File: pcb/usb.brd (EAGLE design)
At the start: 26.2 x 26.2 mm, 27 parts, among them J1 JSTPH, Q1 ZXMP6A13FTA, Q2 mmbt2222, Q3 mmbt2222, U1 MIC5225-3.3v, U2 CH340C, U3 MCP73831T-2ACI/OT, X1 SM02B-SRSS-TB

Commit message: Headers were on the wrong side on the usb board
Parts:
- flipped JP1 to the top
- flipped JP2 to the top
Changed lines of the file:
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@@
 <attribute name="VALUE" x="7.6835" y="9.144" size="0.4064" layer="27" rot="R270"/>
 </element>
-<element name="JP2" library="adafruit" library_urn="urn:adsk.eagle:library:420" package="1X08-CLEANBIG" package3d_urn="urn:adsk.eagle:package:6240708/1" override_package3d_urn="urn:adsk.eagle:package:21520758/2" override_package_urn="urn:adsk.eagle:footprint:6240062/1" value="" x="1.651" y="13.081" smashed="yes" rot="MR90">
-<attribute name="MPN" value="8Fx1L-254mm" x="1.651" y="13.081" size="1.778" layer="28" rot="MR90" display="off"/>
-<attribute name="VALUE" x="-1.524" y="2.921" size="1.27" layer="28" rot="MR90"/>
-</element>
-<element name="JP1" library="adafruit" library_urn="urn:adsk.eagle:library:420" package="1X08-CLEANBIG" package3d_urn="urn:adsk.eagle:package:6240708/1" override_package3d_urn="urn:adsk.eagle:package:21520677/2" override_package_urn="urn:adsk.eagle:footprint:6240062/1" value="" x="24.511" y="13.081" smashed="yes" rot="MR270">
-<attribute name="MPN" value="8Fx1L-254mm" x="24.511" y="13.081" size="1.778" layer="28" rot="MR270" display="off"/>
-<attribute name="VALUE" x="27.686" y="23.241" size="1.27" layer="28" rot="MR270"/>
+<element name="JP2" library="adafruit" library_urn="urn:adsk.eagle:library:420" package="1X08-CLEANBIG" package3d_urn="urn:adsk.eagle:package:6240708/1" override_package3d_urn="urn:adsk.eagle:package:21520758/2" override_package_urn="urn:adsk.eagle:footprint:6240062/1" value="" x="1.651" y="13.081" smashed="yes" rot="R90">
+<attribute name="MPN" value="8Fx1L-254mm" x="1.651" y="13.081" size="1.778" layer="27" rot="R90" display="off"/>
+<attribute name="VALUE" x="4.826" y="2.921" size="1.27" layer="27" rot="R90"/>
+</element>
+<element name="JP1" library="adafruit" library_urn="urn:adsk.eagle:library:420" package="1X08-CLEANBIG" package3d_urn="urn:adsk.eagle:package:6240708/1" override_package3d_urn="urn:adsk.eagle:package:21520677/2" override_package_urn="urn:adsk.eagle:footprint:6240062/1" value="" x="24.511" y="13.081" smashed="yes" rot="R270">
+<attribute name="MPN" value="8Fx1L-254mm" x="24.511" y="13.081" size="1.778" layer="27" rot="R270" display="off"/>
+<attribute name="VALUE" x="21.336" y="23.241" size="1.27" layer="27" rot="R270"/>
 </element>
 <element name="J2" library="Wurth_Elektronik_Electromechanic_Input-Output_Connectors_rev19b_wider_slots" package="614105150621" package3d_urn="urn:adsk.eagle:package:3360156/4" override_package3d_urn="urn:adsk.eagle:package:21520771/2" override_package_urn="urn:adsk.eagle:footprint:21520772/1" value="" x="13.081" y="2.54" smashed="yes" rot="MR0">
@@
 <wire x1="20.0025" y1="18.0975" x2="18.89125" y2="16.98625" width="0.1524" layer="16"/>
 <wire x1="23.1775" y1="18.0975" x2="20.0025" y2="18.0975" width="0.1524" layer="16"/>
-<wire x1="24.28875" y1="19.20875" x2="23.1775" y2="18.0975" width="0.1524" layer="16"/>
-<wire x1="24.28875" y1="19.3675" x2="24.28875" y2="19.20875" width="0.1524" layer="16"/>
-<wire x1="24.4475" y1="19.3675" x2="24.28875" y2="19.3675" width="0.1524" layer="16"/>
-<wire x1="24.4475" y1="19.3675" x2="24.511" y2="19.431" width="0.1524" layer="16"/>
 <via x="16.51" y="12.22375" extent="1-16" drill="0.254"/>
+<wire x1="24.511" y1="19.431" x2="23.1775" y2="18.0975" width="0.1524" layer="16"/>
 </signal>
 <signal name="TX">
@@
 <wire x1="18.51025" y1="20.6375" x2="18.38325" y2="20.5105" width="0.1524" layer="16"/>
 <wire x1="23.1775" y1="20.6375" x2="18.51025" y2="20.6375" width="0.1524" layer="16"/>
-<wire x1="24.28875" y1="21.74875" x2="23.1775" y2="20.6375" width="0.1524" layer="16"/>
-<wire x1="24.28875" y1="21.9075" x2="24.28875" y2="21.74875" width="0.1524" layer="16"/>
-<wire x1="24.4475" y1="21.9075" x2="24.28875" y2="21.9075" width="0.1524" layer="16"/>
 <wire x1="14.605" y1="7.62" x2="14.605" y2="7.614" width="0.1524" layer="1"/>
-<wire x1="24.4475" y1="21.9075" x2="24.511" y2="21.971" width="0.1524" layer="16"/>
 <via x="17.145" y="11.90625" extent="1-16" drill="0.254"/>
 <via x="20.32" y="15.08125" extent="1-16" drill="0.254"/>
@@
 <wire x1="19.0044" y1="16.1906" x2="20.0956875" y2="16.1906" width="0.1524" layer="1"/>
 <wire x1="17.8689" y1="17.7259" x2="17.8689" y2="17.3261" width="0.1524" layer="1"/>
+<wire x1="24.511" y1="21.971" x2="23.1775" y2="20.6375" width="0.1524" layer="16"/>
 </signal>
 <signal name="RESET">
@@
 <wire x1="3.4925" y1="20.16125" x2="3.4925" y2="17.4625" width="0.1524" layer="16"/>
 <wire x1="1.905" y1="21.74875" x2="3.4925" y2="20.16125" width="0.1524" layer="16"/>
-<wire x1="1.905" y1="21.9075" x2="1.905" y2="21.74875" width="0.1524" layer="16"/>
-<wire x1="1.74625" y1="21.9075" x2="1.905" y2="21.9075" width="0.1524" layer="16"/>
 <wire x1="4.1275" y1="11.90625" x2="4.234" y2="11.811" width="0.1524" layer="1"/>
-<wire x1="1.74625" y1="21.9075" x2="1.651" y2="21.971" width="0.1524" layer="16"/>
 <via x="3.96875" y="16.8275" extent="1-16" drill="0.254"/>
+<wire x1="1.651" y1="21.971" x2="1.87325" y2="21.74875" width="0.1524" layer="16"/>
+<wire x1="1.87325" y1="21.74875" x2="1.905" y2="21.74875" width="0.1524" layer="16"/>
 </signal>
 <signal name="RTS">
@@
 <wire x1="24.4475" y1="11.7475" x2="18.0975" y2="11.7475" width="0.1524" layer="16"/>
 <wire x1="9.04875" y1="8.09625" x2="8.974" y2="8.128" width="0.1524" layer="1"/>
-<wire x1="24.4475" y1="11.7475" x2="24.511" y2="11.811" width="0.1524" layer="16"/>
 <via x="9.8425" y="8.09625" extent="1-16" drill="0.254"/>
 <via x="17.78" y="9.04875" extent="1-16" drill="0.254"/>
 <via x="17.93875" y="11.58875" extent="1-16" drill="0.254"/>
+<wire x1="24.511" y1="11.811" x2="24.4475" y2="11.7475" width="0.1524" layer="16"/>
 </signal>
 <signal name="D4/GPIO2">
@@
 <wire x1="6.985" y1="20.0025" x2="6.8881" y2="19.997" width="0.4064" layer="1"/>
 <wire x1="7.14375" y1="17.93875" x2="6.8881" y2="18.097" width="0.4064" layer="1"/>
-<wire x1="23.65375" y1="4.1275" x2="24.4475" y2="4.1275" width="0.4064" layer="16"/>
+<wire x1="24.4475" y1="4.1275" x2="23.65375" y2="4.1275" width="0.4064" layer="16"/>
 <wire x1="17.145" y1="10.63625" x2="23.65375" y2="4.1275" width="0.4064" layer="16"/>
 <wire x1="16.03375" y1="10.63625" x2="17.145" y2="10.63625" width="0.4064" layer="16"/>
 <wire x1="15.5575" y1="11.1125" x2="16.03375" y2="10.63625" width="0.4064" layer="16"/>
 <wire x1="15.5575" y1="12.22375" x2="15.5575" y2="11.1125" width="0.4064" layer="16"/>
-<wire x1="24.4475" y1="4.1275" x2="24.511" y2="4.191" width="0.4064" layer="16"/>
 <wire x1="15.5575" y1="12.22375" x2="15.581" y2="12.35" width="0.4064" layer="16"/>
 <via x="6.985" y="14.2875" extent="1-16" drill="0.254"/>
@@
 <wire x1="7.151" y1="16.002" x2="7.151" y2="14.4535" width="0.4064" layer="1"/>
 <wire x1="7.151" y1="14.4535" x2="6.985" y2="14.2875" width="0.4064" layer="1"/>
+<wire x1="24.511" y1="4.191" x2="24.4475" y2="4.1275" width="0.4064" layer="16"/>
 </signal>
 <signal name="N$2">
@@
 <wire x1="10.61085" y1="10.1346" x2="9.58999375" y2="10.1346" width="0.4064" layer="16"/>
 <wire x1="9.2329" y1="9.77750625" x2="9.2329" y2="9.7409" width="0.4064" layer="16"/>
-<wire x1="3.683" y1="4.191" x2="1.651" y2="4.191" width="0.4064" layer="16"/>
-<wire x1="9.2329" y1="9.7409" x2="3.683" y2="4.191" width="0.4064" layer="16"/>
+<wire x1="3.683" y1="4.191" x2="9.2329" y2="9.7409" width="0.4064" layer="16"/>
 <wire x1="12.054" y1="14.986" x2="12.065" y2="14.975" width="0.4064" layer="1"/>
 <wire x1="12.065" y1="14.975" x2="12.065" y2="13.214" width="0.4064" layer="1"/>
+<wire x1="1.651" y1="4.191" x2="3.683" y2="4.191" width="0.4064" layer="16"/>
 </signal>
 </signals>

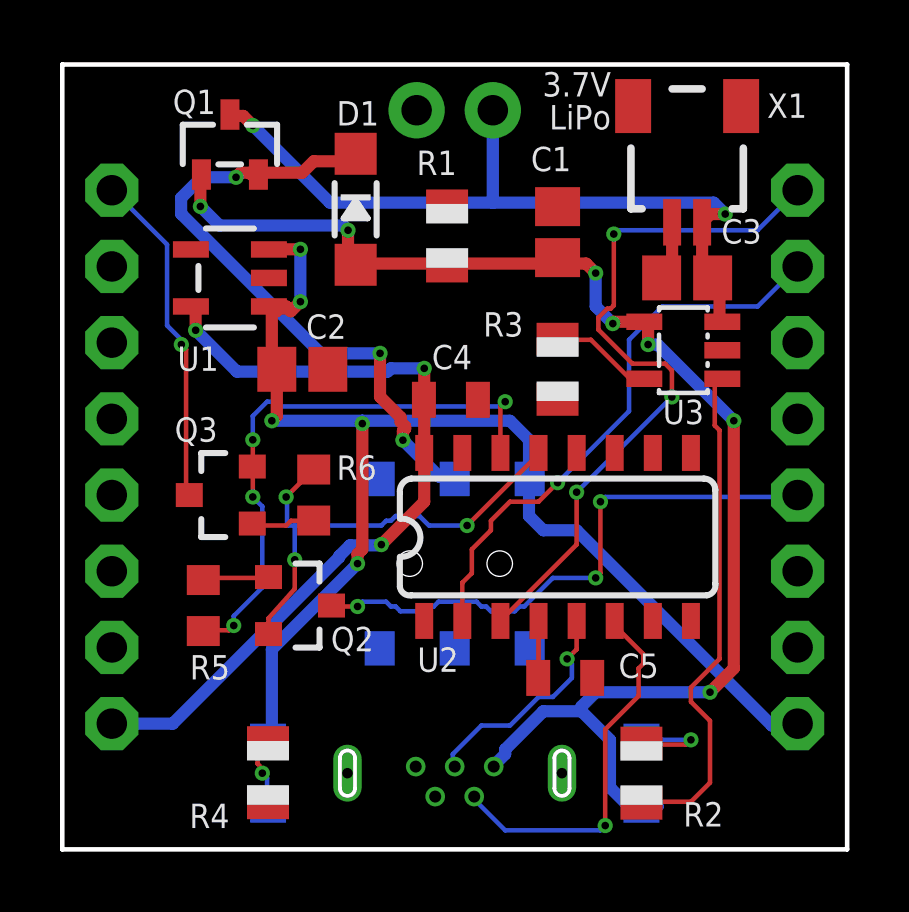
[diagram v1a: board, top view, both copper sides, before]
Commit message: Rotate switch so that pin numbering matches orientation from the datasheet
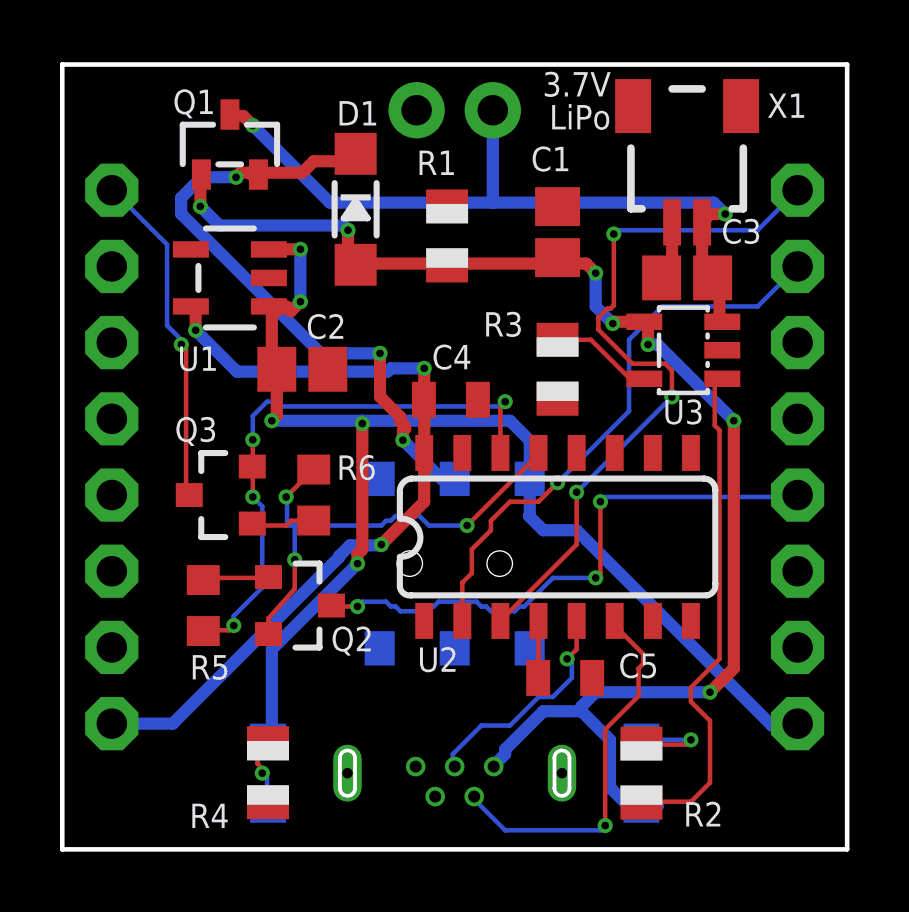
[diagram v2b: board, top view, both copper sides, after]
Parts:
- turned S1 to 180 degrees
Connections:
- net N$7: now also S1.5; no longer S1.2
- net VIN: now also S1.6; no longer S1.1
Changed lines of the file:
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@@
 <attribute name="VALUE" x="7.366" y="22.86" size="0.4064" layer="27" ratio="10"/>
 </element>
-<element name="S1" library="SparkFun-Switches" library_urn="urn:adsk.eagle:library:535" package="SWITCH_DPDT_SMD_AYZ0202" package3d_urn="urn:adsk.eagle:package:40160/1" override_package3d_urn="urn:adsk.eagle:package:21520767/2" override_package_urn="urn:adsk.eagle:footprint:40100/1" value="" x="13.081" y="9.525" smashed="yes" rot="MR0">
-<attribute name="MPN" value="AYZ0202AGRLC" x="13.081" y="9.525" size="1.778" layer="28" rot="MR0" display="off"/>
-<attribute name="NAME" x="17.018" y="11.811" size="0.8128" layer="26" ratio="18" rot="MR0" align="bottom-center"/>
-<attribute name="PROD_ID" value="SWCH-08179" x="13.081" y="9.525" size="1.778" layer="28" rot="MR0" display="off"/>
-<attribute name="SF_ID" value="COM-00597" x="13.081" y="9.525" size="1.778" layer="28" rot="MR0" display="off"/>
-<attribute name="VALUE" x="9.271" y="9.525" size="0.6096" layer="28" font="vector" ratio="20" rot="MR90" align="top-center"/>
+<element name="S1" library="SparkFun-Switches" package="SWITCH_DPDT_SMD_AYZ0202" package3d_urn="urn:adsk.eagle:package:40160/1" override_package3d_urn="urn:adsk.eagle:package:21520767/4" override_package_urn="urn:adsk.eagle:footprint:40100/1" override_locally_modified="yes" value="" x="13.081" y="9.525" smashed="yes" rot="MR180">
+<attribute name="MPN" value="AYZ0202AGRLC" x="13.081" y="9.525" size="1.778" layer="28" rot="MR180" display="off"/>
+<attribute name="NAME" x="16.891" y="12.573" size="0.8128" layer="26" ratio="18" rot="MR180" align="bottom-center"/>
+<attribute name="PROD_ID" value="SWCH-08179" x="13.081" y="9.525" size="1.778" layer="28" rot="MR180" display="off"/>
+<attribute name="SF_ID" value="COM-00597" x="13.081" y="9.525" size="1.778" layer="28" rot="MR180" display="off"/>
+<attribute name="VALUE" x="16.891" y="9.525" size="0.6096" layer="28" font="vector" ratio="20" rot="MR270" align="top-center"/>
 </element>
 <element name="U2" library="SparkFun-IC-Comms" library_urn="urn:adsk.eagle:library:521" package="SO016" value="CH340C" x="16.51" y="10.414" smashed="yes">
@@
 <contactref element="D1" pad="C"/>
 <contactref element="Q1" pad="2"/>
-<contactref element="S1" pad="2"/>
+<contactref element="S1" pad="5"/>
 <wire x1="8.001" y1="22.5552" x2="6.5532" y2="22.5552" width="0.4064" layer="1"/>
 <wire x1="8.382" y1="22.9362" x2="8.001" y2="22.5552" width="0.4064" layer="1"/>
@@
 <wire x1="6.5532" y1="22.5552" x2="6.538" y2="22.495" width="0.4064" layer="1"/>
 <wire x1="9.7536" y1="23.1648" x2="9.779" y2="23.186" width="0.4064" layer="1"/>
-<wire x1="12.573" y1="12.4206" x2="13.0302" y2="12.4206" width="0.4064" layer="16"/>
-<wire x1="11.3538" y1="13.6398" x2="12.573" y2="12.4206" width="0.4064" layer="16"/>
 <wire x1="11.3538" y1="13.9446" x2="11.3538" y2="13.6398" width="0.4064" layer="1"/>
 <wire x1="11.43" y1="14.0208" x2="11.3538" y2="13.9446" width="0.4064" layer="1"/>
@@
 <wire x1="6.2484" y1="22.5552" x2="5.9436" y2="22.5552" width="0.4064" layer="1"/>
 <wire x1="6.3246" y1="22.479" x2="6.2484" y2="22.5552" width="0.4064" layer="1"/>
-<wire x1="13.0302" y1="12.4206" x2="13.081" y2="12.35" width="0.4064" layer="16"/>
 <wire x1="6.3246" y1="22.479" x2="6.538" y2="22.495" width="0.4064" layer="1"/>
 <via x="11.3538" y="13.6398" extent="1-16" drill="0.254"/>
 <via x="10.5918" y="16.5354" extent="1-16" drill="0.254"/>
 <via x="5.7912" y="22.4028" extent="1-16" drill="0.254"/>
+<wire x1="13.081" y1="12.35" x2="12.6436" y2="12.35" width="0.4064" layer="16"/>
+<wire x1="12.6436" y1="12.35" x2="11.3538" y2="13.6398" width="0.4064" layer="16"/>
 </signal>
 <signal name="VIN" class="1">
@@
 <contactref element="U1" pad="1"/>
 <contactref element="U1" pad="3"/>
-<contactref element="S1" pad="1"/>
+<contactref element="S1" pad="6"/>
 <contactref element="ON" pad="A"/>
-<wire x1="15.5575" y1="13.6525" x2="15.5575" y2="12.3825" width="0.4064" layer="16"/>
-<wire x1="14.9225" y1="14.2875" x2="15.5575" y2="13.6525" width="0.4064" layer="16"/>
 <wire x1="6.985" y1="14.2875" x2="10.00125" y2="14.2875" width="0.4064" layer="16"/>
-<wire x1="10.00125" y1="14.2875" x2="14.9225" y2="14.2875" width="0.4064" layer="16"/>
-<wire x1="15.5575" y1="12.3825" x2="15.581" y2="12.35" width="0.4064" layer="16"/>
+<wire x1="14.9225" y1="14.2875" x2="10.00125" y2="14.2875" width="0.4064" layer="16"/>
 <wire x1="6.985" y1="6.6675" x2="6.985" y2="3.65125" width="0.4064" layer="16"/>
 <wire x1="9.8425" y1="9.525" x2="6.985" y2="6.6675" width="0.4064" layer="16"/>
@@
 <wire x1="16.03375" y1="10.63625" x2="17.145" y2="10.63625" width="0.4064" layer="16"/>
 <wire x1="15.5575" y1="11.1125" x2="16.03375" y2="10.63625" width="0.4064" layer="16"/>
-<wire x1="15.5575" y1="12.22375" x2="15.5575" y2="11.1125" width="0.4064" layer="16"/>
-<wire x1="15.5575" y1="12.22375" x2="15.581" y2="12.35" width="0.4064" layer="16"/>
 <via x="6.985" y="14.2875" extent="1-16" drill="0.254"/>
 <via x="9.8425" y="9.525" extent="1-16" drill="0.254"/>
@@
 <wire x1="7.151" y1="14.4535" x2="6.985" y2="14.2875" width="0.4064" layer="1"/>
 <wire x1="24.511" y1="4.191" x2="24.4475" y2="4.1275" width="0.4064" layer="16"/>
+<wire x1="15.581" y1="12.35" x2="15.581" y2="13.629" width="0.4064" layer="16"/>
+<wire x1="15.581" y1="13.629" x2="14.9225" y2="14.2875" width="0.4064" layer="16"/>
+<wire x1="15.581" y1="12.35" x2="15.581" y2="11.136" width="0.4064" layer="16"/>
+<wire x1="15.581" y1="11.136" x2="15.5575" y2="11.1125" width="0.4064" layer="16"/>
 </signal>
 <signal name="N$2">

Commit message: added populate attr
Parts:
- R3: value 10K\ -> 10K
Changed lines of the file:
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@@
 </element>
 <element name="J1" library="SparkFun-Connectors" library_urn="urn:adsk.eagle:library:513" package="1X02" package3d_urn="urn:adsk.eagle:package:38039/1" value="JSTPH" x="14.351" y="24.638" smashed="yes" rot="MR0">
+<attribute name="POPULATE" value="0" x="14.351" y="24.638" size="1.778" layer="28" rot="MR0" display="off"/>
 <attribute name="VALUE" x="15.621" y="22.606" size="0.6096" layer="28" font="vector" ratio="20" rot="MR0"/>
 </element>
@@
 <attribute name="VALUE" x="21.717" y="21.336" size="1.27" layer="27" rot="R180"/>
 </element>
-<element name="R3" library="adafruit" library_urn="urn:adsk.eagle:library:420" package="R0805" package3d_urn="urn:adsk.eagle:package:6240566/1" override_package3d_urn="urn:adsk.eagle:package:21520802/2" override_package_urn="urn:adsk.eagle:footprint:6239920/1" value="10K\" x="16.51" y="16.002" smashed="yes" rot="R270">
+<element name="R3" library="adafruit" library_urn="urn:adsk.eagle:library:420" package="R0805" package3d_urn="urn:adsk.eagle:package:6240566/1" override_package3d_urn="urn:adsk.eagle:package:21520802/2" override_package_urn="urn:adsk.eagle:footprint:6239920/1" value="10K" x="16.51" y="16.002" smashed="yes" rot="R270">
 <attribute name="MPN" value="CRCW080510K0FKEAC" x="16.51" y="16.002" size="1.778" layer="27" rot="R270" display="off"/>
 <attribute name="NAME" x="15.367" y="17.907" size="0.8128" layer="25" rot="R180"/>
